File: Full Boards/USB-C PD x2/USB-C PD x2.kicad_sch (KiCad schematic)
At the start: 160 parts, among them J1 Conn_02x05_Odd_Even, J2 Conn_01x05_Pin

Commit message: Updated the USB-C PD board to add Part to symbols that need it and and marked test points as DNP/EFBoM.
Signed-off-by: digimer <digital.mermaid@gmail.com>
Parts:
- J1: Part (none) -> Sullins GRPB052VWVN-RC
- J2: Part (none) -> Amphenol 68001-416HLF; now left out of the parts list
- TP1, TP2: Part (none) -> Amphenol 68001-416HLF; now not fitted; now left out of the parts list
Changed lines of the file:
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@@
 		(body_style 1)
 		(exclude_from_sim no)
-		(in_bom yes)
-		(on_board yes)
-		(in_pos_files yes)
-		(dnp no)
+		(in_bom no)
+		(on_board yes)
+		(in_pos_files yes)
+		(dnp yes)
 		(property "Reference" "TP2"
 			(at 162.306 45.72 0)
@@
 			)
 		)
+		(property "Part" "Amphenol 68001-416HLF"
+			(at 163.83 50.8 0)
+			(hide yes)
+			(show_name no)
+			(do_not_autoplace no)
+			(effects
+				(font
+					(size 1.27 1.27)
+				)
+			)
+		)
 		(pin "1"
 		)
@@
 		(body_style 1)
 		(exclude_from_sim no)
-		(in_bom yes)
-		(on_board yes)
-		(in_pos_files yes)
-		(dnp no)
+		(in_bom no)
+		(on_board yes)
+		(in_pos_files yes)
+		(dnp yes)
 		(property "Reference" "TP1"
 			(at 119.126 45.72 0)
@@
 		)
 		(property "Description" "test point"
+			(at 120.65 50.8 0)
+			(hide yes)
+			(show_name no)
+			(do_not_autoplace no)
+			(effects
+				(font
+					(size 1.27 1.27)
+				)
+			)
+		)
+		(property "Part" "Amphenol 68001-416HLF"
 			(at 120.65 50.8 0)
 			(hide yes)
@@
 		(body_style 1)
 		(exclude_from_sim no)
-		(in_bom yes)
+		(in_bom no)
 		(on_board yes)
 		(in_pos_files yes)
@@
 			)
 		)
+		(property "Part" "Amphenol 68001-416HLF"
+			(at 209.55 31.75 0)
+			(hide yes)
+			(show_name no)
+			(do_not_autoplace no)
+			(effects
+				(font
+					(size 1.27 1.27)
+				)
+			)
+		)
 		(pin "2"
 		)
@@
 			(at 219.71 77.47 0)
 			(hide yes)
+			(show_name no)
+			(do_not_autoplace no)
+			(effects
+				(font
+					(size 1.27 1.27)
+				)
+			)
+		)
+		(property "Part" "Sullins GRPB052VWVN-RC"
+			(at 219.71 77.47 0)
+			(hide yes)

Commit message: Added metadata for the Diodes Inc DMTH45M5LPSWQ-13
Signed-off-by: digimer <digital.mermaid@gmail.com>
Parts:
- TR1, TR10, TR11, TR12, TR2, TR3, TR4, TR5, TR6, TR7, TR8, TR9: Part (none) -> Diodes Inc DMTH45M5LPSWQ-13
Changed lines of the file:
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@@
 			)
 		)
-		(property "Datasheet" ""
+		(property "Datasheet" "https://www.diodes.com/assets/Datasheets/DMTH45M5LPSWQ.pdf"
 			(at 34.29 159.258 0)
 			(hide yes)
@@
 			)
 		)
-		(property "Description" ""
+		(property "Description" "N-Channel 40 V 86A (Tc) 3.5W (Ta), 72W (Tc) Surface Mount, Wettable Flank PowerDI5060-8 (Type UX)"
 			(at 34.29 149.86 0)
 			(hide yes)
@@
 			)
 		)
+		(property "Part" "Diodes Inc DMTH45M5LPSWQ-13"
+			(at 34.29 165.1 0)
+			(hide yes)
+			(show_name no)
+			(do_not_autoplace no)
+			(effects
+				(font
+					(size 1.27 1.27)
+				)
+			)
+		)
 		(pin "8"
 		)
@@
 			)
 		)
-		(property "Datasheet" ""
+		(property "Datasheet" "https://www.diodes.com/assets/Datasheets/DMTH45M5LPSWQ.pdf"
 			(at 83.82 265.938 0)
 			(hide yes)
@@
 			)
 		)
-		(property "Description" ""
+		(property "Description" "N-Channel 40 V 86A (Tc) 3.5W (Ta), 72W (Tc) Surface Mount, Wettable Flank PowerDI5060-8 (Type UX)"
 			(at 83.82 256.54 0)
 			(hide yes)
@@
 			)
 		)
+		(property "Part" "Diodes Inc DMTH45M5LPSWQ-13"
+			(at 83.82 271.78 0)
+			(hide yes)
+			(show_name no)
+			(do_not_autoplace no)
+			(effects
+				(font
+					(size 1.27 1.27)
+				)
+			)
+		)
 		(pin "8"
 		)
@@
 			)
 		)
-		(property "Datasheet" ""
+		(property "Datasheet" "https://www.diodes.com/assets/Datasheets/DMTH45M5LPSWQ.pdf"
 			(at 182.88 194.818 0)
 			(hide yes)
@@
 			)
 		)
-		(property "Description" ""
+		(property "Description" "N-Channel 40 V 86A (Tc) 3.5W (Ta), 72W (Tc) Surface Mount, Wettable Flank PowerDI5060-8 (Type UX)"
 			(at 182.88 185.42 0)
 			(hide yes)
@@
 			)
 		)
+		(property "Part" "Diodes Inc DMTH45M5LPSWQ-13"
+			(at 182.88 200.66 0)
+			(hide yes)
+			(show_name no)
+			(do_not_autoplace no)
+			(effects
+				(font
+					(size 1.27 1.27)
+				)
+			)
+		)
 		(pin "8"
 		)
@@
 			)
 		)
-		(property "Datasheet" ""
+		(property "Datasheet" "https://www.diodes.com/assets/Datasheets/DMTH45M5LPSWQ.pdf"
 			(at 199.39 265.938 0)
 			(hide yes)
@@
 			)
 		)
-		(property "Description" ""
+		(property "Description" "N-Channel 40 V 86A (Tc) 3.5W (Ta), 72W (Tc) Surface Mount, Wettable Flank PowerDI5060-8 (Type UX)"
 			(at 199.39 256.54 0)
 			(hide yes)
@@
 			)
 		)
+		(property "Part" "Diodes Inc DMTH45M5LPSWQ-13"
+			(at 199.39 271.78 0)
+			(hide yes)
+			(show_name no)
+			(do_not_autoplace no)
+			(effects
+				(font
+					(size 1.27 1.27)
+				)
+			)
+		)
 		(pin "8"
 		)
@@
 			)
 		)
-		(property "Datasheet" ""
+		(property "Datasheet" "https://www.diodes.com/assets/Datasheets/DMTH45M5LPSWQ.pdf"
 			(at 182.88 159.258 0)
 			(hide yes)
@@
 			)
 		)
-		(property "Description" ""
+		(property "Description" "N-Channel 40 V 86A (Tc) 3.5W (Ta), 72W (Tc) Surface Mount, Wettable Flank PowerDI5060-8 (Type UX)"
 			(at 182.88 149.86 0)
 			(hide yes)
@@
 			)
 		)
+		(property "Part" "Diodes Inc DMTH45M5LPSWQ-13"
+			(at 182.88 165.1 0)
+			(hide yes)
+			(show_name no)
+			(do_not_autoplace no)
+			(effects
+				(font
+					(size 1.27 1.27)
+				)
+			)
+		)
 		(pin "8"
 		)
@@
 			)
 		)
-		(property "Datasheet" ""
+		(property "Datasheet" "https://www.diodes.com/assets/Datasheets/DMTH45M5LPSWQ.pdf"
 			(at 139.7 159.258 0)
 			(hide yes)
@@
 			)
 		)
-		(property "Description" ""
+		(property "Description" "N-Channel 40 V 86A (Tc) 3.5W (Ta), 72W (Tc) Surface Mount, Wettable Flank PowerDI5060-8 (Type UX)"
 			(at 139.7 149.86 0)
 			(hide yes)
@@
 			)
 		)
+		(property "Part" "Diodes Inc DMTH45M5LPSWQ-13"
+			(at 139.7 165.1 0)
+			(hide yes)
+			(show_name no)
+			(do_not_autoplace no)
+			(effects
+				(font
+					(size 1.27 1.27)
+				)
+			)
+		)
 		(pin "8"
 		)
@@
 			)
 		)
-		(property "Datasheet" ""
+		(property "Datasheet" "https://www.diodes.com/assets/Datasheets/DMTH45M5LPSWQ.pdf"
 			(at 139.7 194.818 0)
 			(hide yes)
@@
 			)
 		)
-		(property "Description" ""
+		(property "Description" "N-Channel 40 V 86A (Tc) 3.5W (Ta), 72W (Tc) Surface Mount, Wettable Flank PowerDI5060-8 (Type UX)"
 			(at 139.7 185.42 0)
 			(hide yes)
@@
 			)
 		)
+		(property "Part" "Diodes Inc DMTH45M5LPSWQ-13"
+			(at 139.7 200.66 0)
+			(hide yes)
+			(show_name no)
+			(do_not_autoplace no)
+			(effects
+				(font
+					(size 1.27 1.27)
+				)
+			)
+		)
 		(pin "8"
 		)
@@
 			)
 		)
-		(property "Datasheet" ""
+		(property "Datasheet" "https://www.diodes.com/assets/Datasheets/DMTH45M5LPSWQ.pdf"
 			(at 106.68 247.142 0)
 			(hide yes)
@@
 			)
 		)
-		(property "Description" ""
+		(property "Description" "N-Channel 40 V 86A (Tc) 3.5W (Ta), 72W (Tc) Surface Mount, Wettable Flank PowerDI5060-8 (Type UX)"
 			(at 106.68 256.54 0)
 			(hide yes)
@@
 			)
 		)
+		(property "Part" "Diodes Inc DMTH45M5LPSWQ-13"
+			(at 106.68 241.3 0)
+			(hide yes)
+			(show_name no)
+			(do_not_autoplace no)
+			(effects
+				(font
+					(size 1.27 1.27)
+				)
+			)
+		)
 		(pin "8"
 		)
@@
 			)
 		)
-		(property "Datasheet" ""
+		(property "Datasheet" "https://www.diodes.com/assets/Datasheets/DMTH45M5LPSWQ.pdf"
 			(at 34.29 193.548 0)
 			(hide yes)
@@
 			)
 		)
-		(property "Description" ""
+		(property "Description" "N-Channel 40 V 86A (Tc) 3.5W (Ta), 72W (Tc) Surface Mount, Wettable Flank PowerDI5060-8 (Type UX)"
 			(at 34.29 184.15 0)
 			(hide yes)
@@
 			)
 		)
+		(property "Part" "Diodes Inc DMTH45M5LPSWQ-13"
+			(at 34.29 199.39 0)
+			(hide yes)
+			(show_name no)
+			(do_not_autoplace no)
+			(effects
+				(font
+					(size 1.27 1.27)
+				)
+			)
+		)
 		(pin "8"
 		)
@@
 			)
 		)
-		(property "Datasheet" ""
+		(property "Datasheet" "https://www.diodes.com/assets/Datasheets/DMTH45M5LPSWQ.pdf"
 			(at 222.25 247.142 0)
 			(hide yes)
@@
 			)
 		)
-		(property "Description" ""
+		(property "Description" "N-Channel 40 V 86A (Tc) 3.5W (Ta), 72W (Tc) Surface Mount, Wettable Flank PowerDI5060-8 (Type UX)"
 			(at 222.25 256.54 0)
 			(hide yes)
@@
 			)
 		)
+		(property "Part" "Diodes Inc DMTH45M5LPSWQ-13"
+			(at 222.25 241.3 0)
+			(hide yes)
+			(show_name no)
+			(do_not_autoplace no)
+			(effects
+				(font
+					(size 1.27 1.27)
+				)
+			)
+		)
 		(pin "8"
 		)
@@
 			)
 		)
-		(property "Datasheet" ""
+		(property "Datasheet" "https://www.diodes.com/assets/Datasheets/DMTH45M5LPSWQ.pdf"
 			(at 77.47 159.258 0)
 			(hide yes)
@@
 			)
 		)
-		(property "Description" ""
+		(property "Description" "N-Channel 40 V 86A (Tc) 3.5W (Ta), 72W (Tc) Surface Mount, Wettable Flank PowerDI5060-8 (Type UX)"
 			(at 77.47 149.86 0)
 			(hide yes)
@@
 			)
 		)
+		(property "Part" "Diodes Inc DMTH45M5LPSWQ-13"
+			(at 77.47 165.1 0)
+			(hide yes)
+			(show_name no)
+			(do_not_autoplace no)
+			(effects
+				(font
+					(size 1.27 1.27)
+				)
+			)
+		)
 		(pin "8"
 		)
@@
 			)
 		)
-		(property "Datasheet" ""
+		(property "Datasheet" "https://www.diodes.com/assets/Datasheets/DMTH45M5LPSWQ.pdf"
 			(at 77.47 194.818 0)
 			(hide yes)
@@
 			)
 		)
-		(property "Description" ""
+		(property "Description" "N-Channel 40 V 86A (Tc) 3.5W (Ta), 72W (Tc) Surface Mount, Wettable Flank PowerDI5060-8 (Type UX)"
 			(at 77.47 185.42 0)
 			(hide yes)
 			(show_name no)
+			(do_not_autoplace no)
+			(effects
+				(font
+					(size 1.27 1.27)
+				)
+			)
+		)
+		(property "Part" "Diodes Inc DMTH45M5LPSWQ-13"
+			(at 77.47 200.66 0)
+			(hide yes)
+			(show_name no)

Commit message: Update GCT USB4105-GF-A's metadata
Signed-off-by: digimer <digital.mermaid@gmail.com>
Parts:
- USBR1, USBR2: MANUFACTURER GCT -> (none); MAXIMUM_PACKAGE_HEIGHT 3.31 mm -> (none); PARTREV B4 -> (none); Part (none) -> GCT USB4105-GF-A; STANDARD Manufacturer Recommendations -> (none)
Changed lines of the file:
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@@
 			)
 		)
-		(property "PARTREV" "B4"
-			(at 122.174 252.73 0)
-			(hide yes)
-			(show_name no)
-			(do_not_autoplace no)
-			(effects
-				(font
-					(size 1.27 1.27)
-				)
-				(justify bottom)
-			)
-		)
-		(property "STANDARD" "Manufacturer Recommendations"
-			(at 119.888 234.95 0)
-			(hide yes)
-			(show_name no)
-			(do_not_autoplace no)
-			(effects
-				(font
-					(size 1.27 1.27)
-				)
-				(justify bottom)
-			)
-		)
-		(property "MAXIMUM_PACKAGE_HEIGHT" "3.31 mm"
-			(at 122.174 259.08 0)
-			(hide yes)
-			(show_name no)
-			(do_not_autoplace no)
-			(effects
-				(font
-					(size 1.27 1.27)
-				)
-				(justify bottom)
-			)
-		)
-		(property "MANUFACTURER" "GCT"
-			(at 122.174 212.344 0)
+		(property "Part" "GCT USB4105-GF-A"
+			(at 119.634 234.95 0)
 			(hide yes)
 			(show_name no)
@@
 			)
 		)
-		(property "PARTREV" "B4"
-			(at 6.604 252.73 0)
-			(hide yes)
-			(show_name no)
-			(do_not_autoplace no)
-			(effects
-				(font
-					(size 1.27 1.27)
-				)
-				(justify bottom)
-			)
-		)
-		(property "STANDARD" "Manufacturer Recommendations"
-			(at 4.318 234.95 0)
-			(hide yes)
-			(show_name no)
-			(do_not_autoplace no)
-			(effects
-				(font
-					(size 1.27 1.27)
-				)
-				(justify bottom)
-			)
-		)
-		(property "MAXIMUM_PACKAGE_HEIGHT" "3.31 mm"
-			(at 6.604 259.08 0)
-			(hide yes)
-			(show_name no)
-			(do_not_autoplace no)
-			(effects
-				(font
-					(size 1.27 1.27)
-				)
-				(justify bottom)
-			)
-		)
-		(property "MANUFACTURER" "GCT"
-			(at 6.604 212.344 0)
+		(property "Part" "GCT USB4105-GF-A"
+			(at 4.064 234.95 0)
 			(hide yes)
 			(show_name no)

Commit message: Updated Infineon CYPD727268LQXQXQSA1 metadata.
Signed-off-by: digimer <digital.mermaid@gmail.com>
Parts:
- NTC1, NTC2: Part (none) -> Vishay NTCS0805E3103FHT
- PD1: footprint mr-stuff:Infineon CYPD727x -> Package_DFN_QFN:QFN-68-1EP_8x8mm_P0.4mm_EP5.2x5.2mm_ThermalVias; Part (none) -> Infineon CYPD727268LQXQXQSA1
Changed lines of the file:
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@@
 			)
 		)
-		(property "Footprint" "mr-stuff:Infineon CYPD727x"
+		(property "Footprint" "Package_DFN_QFN:QFN-68-1EP_8x8mm_P0.4mm_EP5.2x5.2mm_ThermalVias"
 			(at 339.344 156.718 0)
 			(hide yes)
@@
 			)
 		)
+		(property "Part" "Infineon CYPD727268LQXQXQSA1"
+			(at 339.09 154.178 0)
+			(hide yes)
+			(show_name no)
+			(do_not_autoplace no)
+			(effects
+				(font
+					(size 1.27 1.27)
+				)
+			)
+		)
 		(pin "61"
 		)
@@
 			)
 		)
+		(property "Part" "Vishay NTCS0805E3103FHT"
+			(at 283.718 129.54 0)
+			(hide yes)
+			(show_name no)
+			(do_not_autoplace no)
+			(effects
+				(font
+					(size 1.27 1.27)
+				)
+			)
+		)
 		(pin "1"
 		)
@@
 			(hide yes)
 			(show_name no)
+			(do_not_autoplace no)
+			(effects
+				(font
+					(size 1.27 1.27)
+				)
+			)
+		)
+		(property "Part" "Vishay NTCS0805E3103FHT"
+			(at 267.208 129.54 0)
+			(hide yes)
+			(show_name no)

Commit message: Bulk updated metadata to add Part to all parts.
Signed-off-by: digimer <digital.mermaid@gmail.com>
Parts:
- C1: value 0.22μF -> 0.22uF; Part (none) -> Kyocera 08055C224J4Z2A
- C10, C11, C12, C14, C15, C18, C19, C20, C36, C6, C7: value 10μF -> 10uF; Part (none) -> TDK CGA5L1X7R1H106K160AE
- C13, C17, C23, C26, C27, C28, C29, C30, C31, C33, C35, C37, C39, C40, C41, C42, C45, C46, C47, C48, C49, C5, C9: value 0.1μF -> 0.1uF; Part (none) -> Kyocera 08051C104K4Z2A
- C16, C8: value 68µF -> 68uF; Part (none) -> Nichicon GXC1H680MCW1GS
- C2: value 3.3nF -> 3300pF; Part (none) -> Kyocera KAM21BR71H332JT
- C21, C22, C24, C25: Part (none) -> Yageo AC0805JRNPO9BN391
- C3, C4: value 330 µF -> 330 uF
- C32, C38, C43, C44: value 1μF -> 1uF; Part (none) -> Kyocera 08051C105K4Z2A
- C_OUT_1_0, C_OUT_1_1, C_OUT_2_0, C_OUT_2_1, C_OUT_3_0, C_OUT_3_1: value 330 µF -> 330 uF; Part (none) -> Panasonic EEH-ZU1V331V
- Cc1: value 10nF -> 0.01uF; Part (none) -> Kemet C1206C103J3RACAUTO
- Cc2: value 470nF -> 0.470uF; Part (none) -> Kemet C1206C474J3RACAUTO
- Cp1: Part (none) -> Kemet C0805C221J5GACAUTO
- Cp2: value 1.5nF -> 1500pF; Part (none) -> Kemet C0805C152J5GACAUTO
- D3, D4, D5, D6: Part (none) -> Nexperia PMEG40T10ERX
- L1, L2: Part (none) -> Codaca CSBL1809-100M
- LED1, LED2, LED3, LED4: Part (none) -> Vishay TLMS1101-GS15
- PR1, PR2, Rc2: Part (none) -> Stackpole RNCP1206FTD2K21
- R10, R13, R14, R15, R16, R7, R8, R9: Part (none) -> Stackpole RNCP0805FTD10R0
- R11, R12, R5, R6: Part (none) -> Vishay WSLP25125L000FEA
- R17, R18, R19, R24: Part (none) -> Stackpole RNCP1206FTD10K0
- R20, R21, R22, R23: Part (none) -> Stackpole RNCP0805FTD681R
- R25: Part (none) -> See Config Note on Schematic; now not fitted; now left out of the parts list
- Rc1: Part (none) -> Stackpole RNCP1206FTD20K0
- TP10, TP11, TP3, TP4, TP5, TP6, TP7, TP8, TP9: Part (none) -> Amphenol 68001-416HLF; now not fitted; now left out of the parts list
- TVS2, TVS3, TVS4, TVS5, TVS6, TVS7, TVS8, TVS9: Part (none) -> Nexperia PESD24VU1UT,215

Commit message: Clarified variant in Part for LTC4368IMS-1#PBF
Signed-off-by: digimer <digital.mermaid@gmail.com>
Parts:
- PMIC1: Part ADI LTC4368 -> ADI LTC4368IMS-1#PBF
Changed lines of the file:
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@@
 		(title "USB-C PC 2x 100W")
 		(date "2026-08-13")
-		(rev "v1.3.2")
+		(rev "v1.3.3")
 		(company "The Digital Mermaid")
 	)
@@
 			)
 		)
-		(property "Part" "ADI LTC4368"
+		(property "Part" "ADI LTC4368IMS-1#PBF"
 			(at 49.53 78.74 0)
 			(hide yes)
@@
 			)
 		)
-		(property "Arrow Part Number" ""
-			(at 49.53 52.07 0)
-			(hide yes)
-			(show_name no)
-			(do_not_autoplace no)
-			(effects
-				(font
-					(size 1.27 1.27)
-				)
-			)
-		)
-		(property "Arrow Price/Stock" ""
-			(at 49.53 52.07 0)
-			(hide yes)
-			(show_name no)
-			(do_not_autoplace no)
-			(effects
-				(font
-					(size 1.27 1.27)
-				)
-			)
-		)
-		(property "Height" ""
-			(at 49.53 52.07 0)
-			(hide yes)
-			(show_name no)
-			(do_not_autoplace no)
-			(effects
-				(font
-					(size 1.27 1.27)
-				)
-			)
-		)
-		(property "Manufacturer_Name" ""
-			(at 49.53 52.07 0)
-			(hide yes)
-			(show_name no)
-			(do_not_autoplace no)
-			(effects
-				(font
-					(size 1.27 1.27)
-				)
-			)
-		)
-		(property "Manufacturer_Part_Number" ""
-			(at 49.53 52.07 0)
-			(hide yes)
-			(show_name no)
-			(do_not_autoplace no)
-			(effects
-				(font
-					(size 1.27 1.27)
-				)
-			)
-		)
-		(property "Mouser Part Number" ""
-			(at 49.53 52.07 0)
-			(hide yes)
-			(show_name no)
-			(do_not_autoplace no)
-			(effects
-				(font
-					(size 1.27 1.27)
-				)
-			)
-		)
-		(property "Mouser Price/Stock" ""
-			(at 49.53 52.07 0)
-			(hide yes)
-			(show_name no)
-			(do_not_autoplace no)
-			(effects
-				(font
-					(size 1.27 1.27)
-				)
-			)
-		)

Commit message: Added `Alt Part` to the symbols I ordered alternates for due to stock constraints.
Signed-off-by: digimer <digital.mermaid@gmail.com>
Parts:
- LED1, LED2, LED3, LED4: Alt Part (none) -> ams OSRAM LS Q976.01-N1Q2-1-20-R18
- R2: Alt Part (none) -> Stackpole RNCP1206FTD51K1
- TVS2, TVS3, TVS4, TVS5, TVS6, TVS7, TVS8, TVS9: Alt Part (none) -> Vishay VGSOT24-HG3-08; Part Number PESD24VU1UT,215 -> (none)

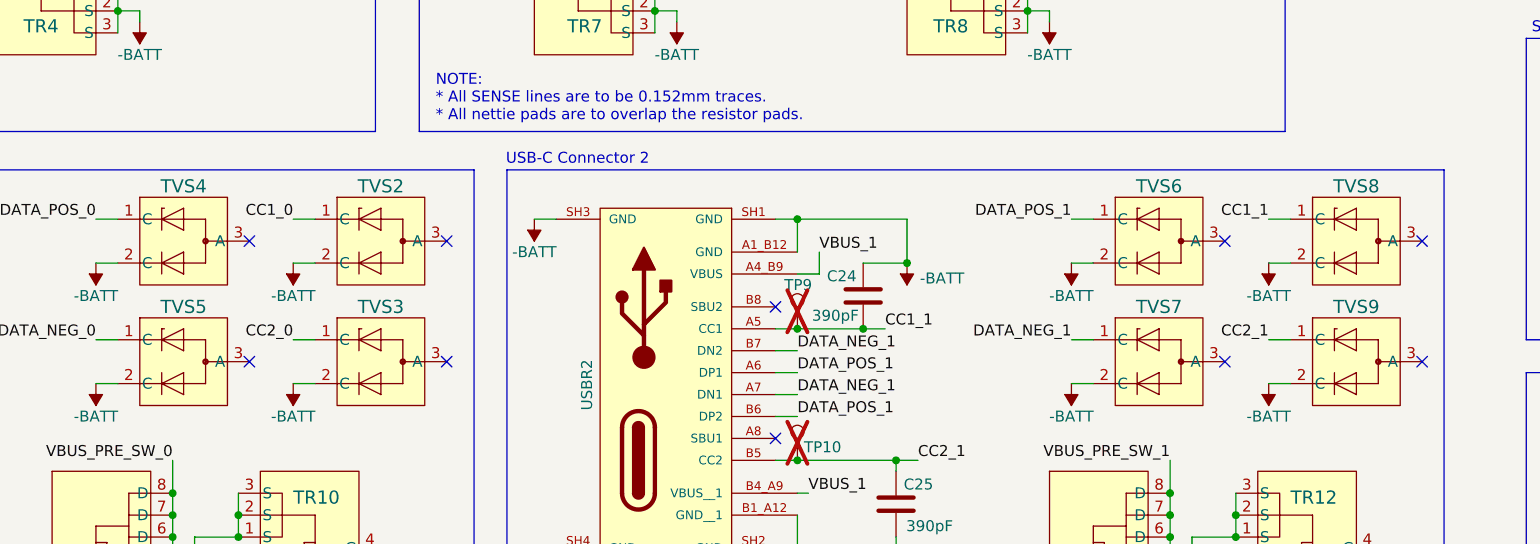
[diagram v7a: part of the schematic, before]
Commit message: Fixed the TVS diode used for the USB cables to a dual-zener variant. Removed `Alt Part` and switched the LED and R2 to the parts I orderd.
Signed-off-by: digimer <digital.mermaid@gmail.com>
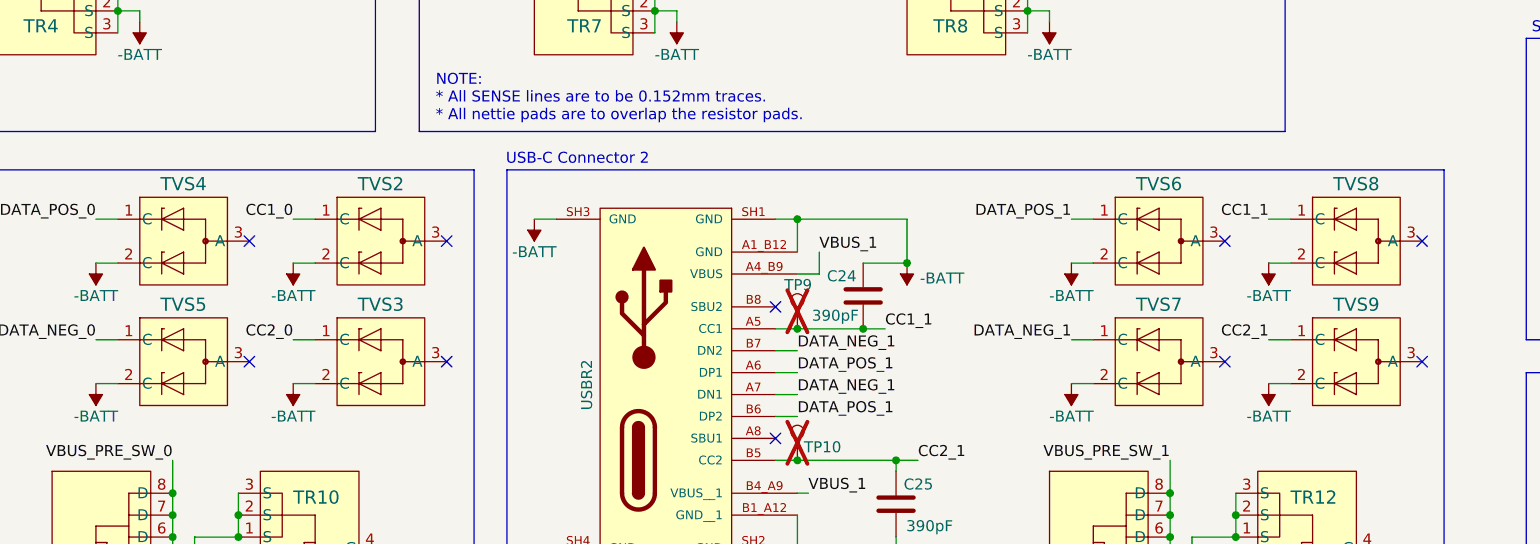
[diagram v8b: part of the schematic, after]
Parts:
- LED1, LED2, LED3, LED4: footprint LED_SMD:LED_0603_1608Metric -> mr-stuff:ams OSRAM LS Q976.01; Alt Part ams OSRAM LS Q976.01-N1Q2-1-20-R18 -> (none); Part Vishay TLMS1101-GS15 -> ams OSRAM LS Q976.01-N1Q2-1-20-R18
- R2: Alt Part Stackpole RNCP1206FTD51K1 -> (none); Part Stackpole RMCF1206FG51K1 -> Stackpole RNCP1206FTD51K1
- TVS2, TVS3, TVS4, TVS5, TVS6, TVS7, TVS8, TVS9: footprint mr-stuff:Nexperia PESD24 -> mr-stuff:Nexperia MMBZ27; symbol mr-parts:Nexperia PESD24 -> mr-parts:Nexperia MMBZ27; Alt Part Vishay VGSOT24-HG3-08 -> (none); Part Nexperia PESD24VU1UT,215 -> Nexperia MMBZ27VAL,215
